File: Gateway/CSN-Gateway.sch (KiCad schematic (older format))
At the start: 42 parts, among them IC1 ATMEGA328-A, P1 CONN_DEBUG, P2 CONN_01X02, P3 CONN_ICSP, P4 CONN_OLED_SCREEN, P5 YHDC_SCT-013, P6 YHDC_SCT-013, P7 YHDC_SCT-013, P8 CONN_NRF24L01, P9 CONN_RS485, SW1 SW_PUSH, U1 MAX485CSA, U2 AMS1117-3.3, Y1 Crystal

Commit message: More work on gateway
- Add ftdi ft232rl chip for usb comms
- Remove debug connector (not used if we have usb)
- Add capa and resistors to rs485
- Draw edge cut for both bottom and top pcb at the correct size of the
case
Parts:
- removed P1: CONN_DEBUG, symbol CONN_01X06
- added C12: 0.1uF, symbol C
- added C13: 10uF, symbol C
- added IC2: FT232RL, SSOP28-LD, symbol FT232RL
- added P1: USB_MINI, symbol USB_OTG
- added R17, R18: 20K, symbol R
- added R19: 120, symbol R
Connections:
- net labels removed: DTR
- wire segments 176 -> 201
- no-connect marks 2 -> 18
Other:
- moved on the sheet: C1, C10, C11, C3, C4, C5, C6, C7, C8, C9, D1, IC1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

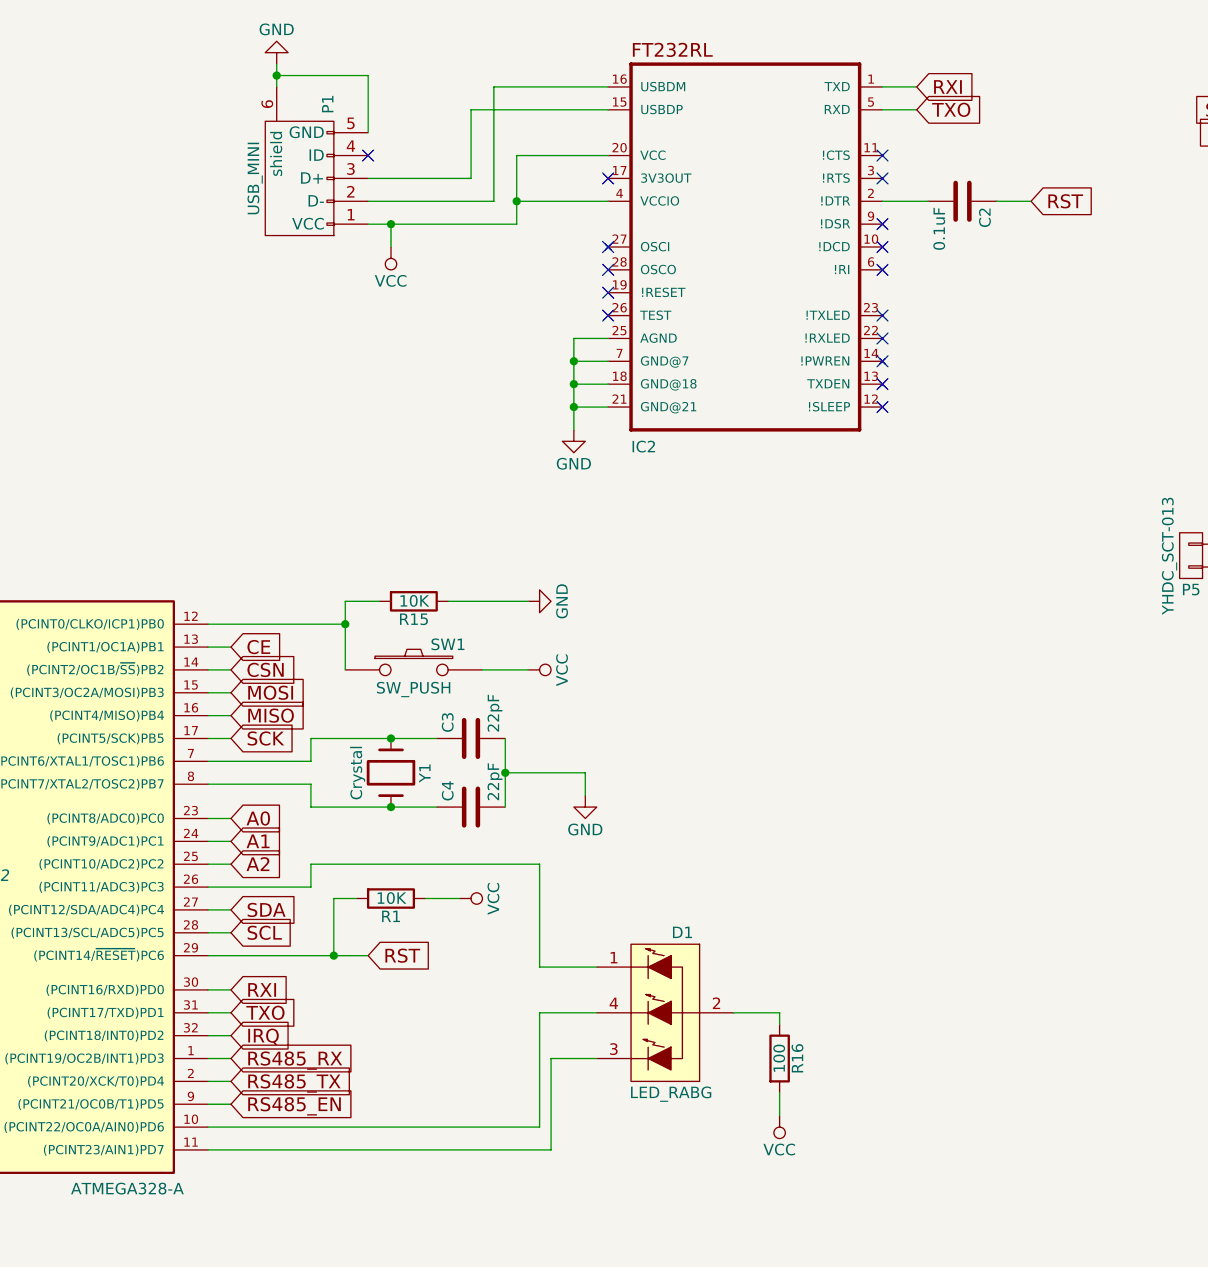
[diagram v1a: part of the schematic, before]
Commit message: FT232R in Self powered mode + switch button
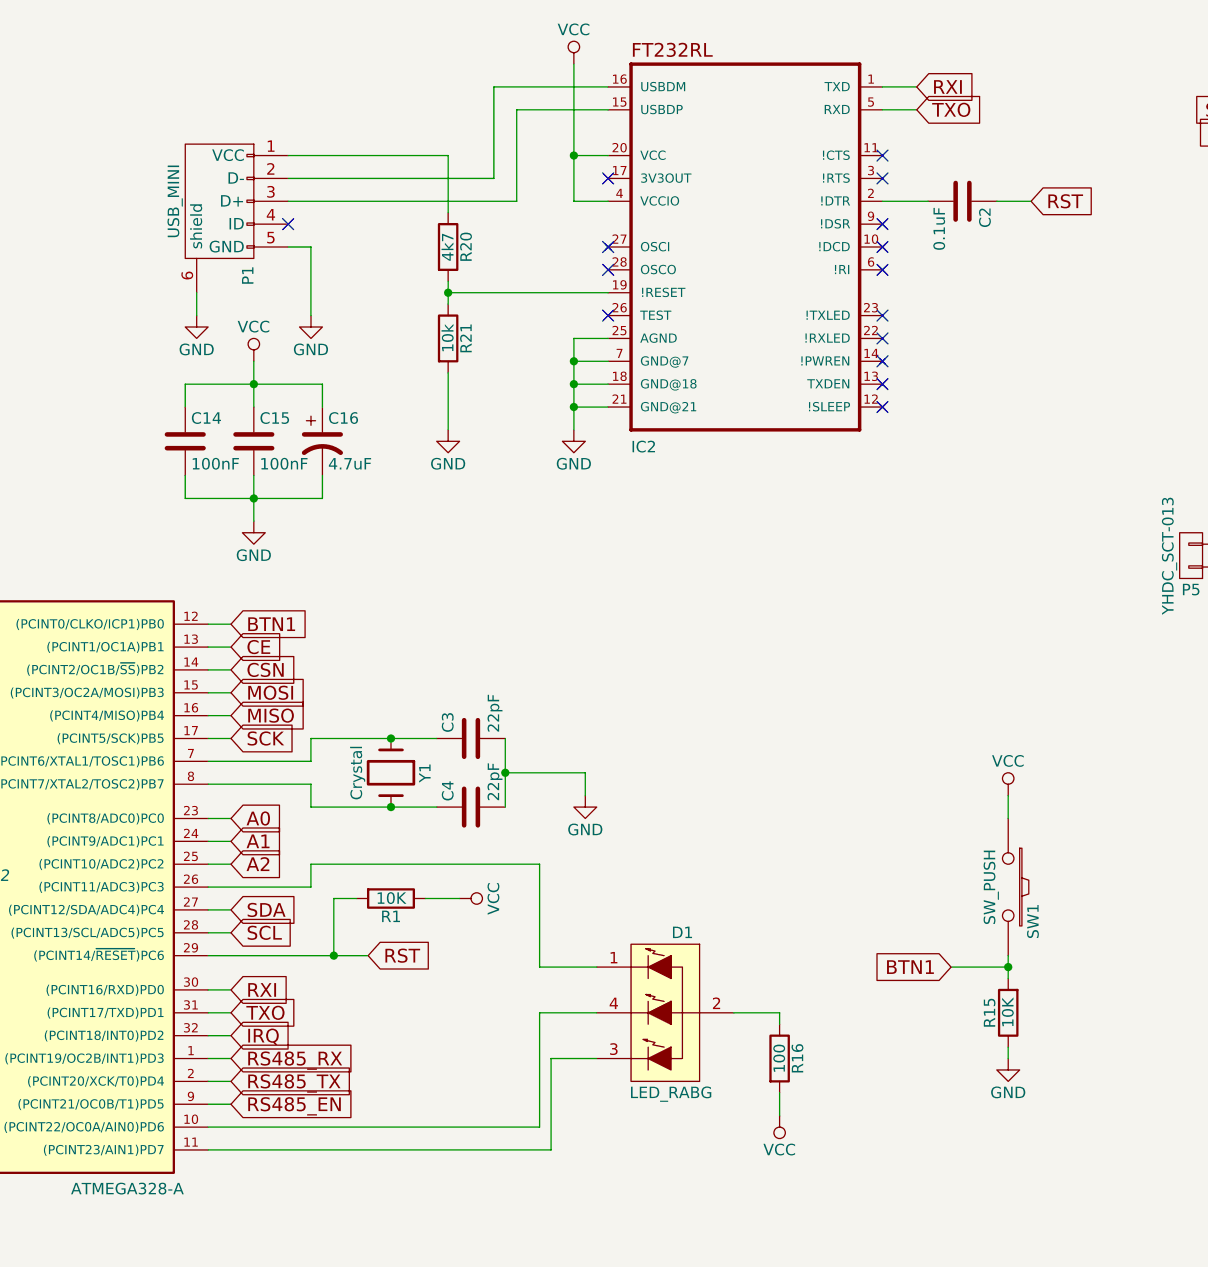
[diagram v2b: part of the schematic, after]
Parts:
- added C14, C15: 100nF, symbol C
- added C16: 4.7uF, symbol CP1
- added R20: 4k7, symbol R
- added R21: 10k, symbol R
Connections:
- net GND: now also C14.2, C15.2, C16.2, R21.2
- net VCC: now also SW1.1, C14.1, C15.1, C16.1; no longer P1.1 (VCC), SW1.2
- net BTN1: now reaches IC1.12 ((PCINT0/CLKO/ICP1)PB0), R15.2
- net BTN1: now also SW1.2; no longer SW1.1
- net at IC2.19 (!RESET): now also R20.2, R21.1
- new net: P1.1 (VCC), R20.1
- no-connect marks 18 -> 17
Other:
- moved on the sheet: P1, R15, SW1

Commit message: Change capa
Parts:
- C10, C13, C9: symbol C -> CP1
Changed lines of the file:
@@
 $EndComp
 $Comp
-L GND #PWR3
+L GND #PWR01
 U 1 1 582C3EF1
 P 1350 5550
-F 0 "#PWR3" H 1350 5300 50  0001 C CNN
+F 0 "#PWR01" H 1350 5300 50  0001 C CNN
 F 1 "GND" H 1350 5400 50  0000 C CNN
 F 2 "" H 1350 5550 50  0000 C CNN
@@
 $EndComp
 $Comp
-L GND #PWR20
+L GND #PWR02
 U 1 1 582C410C
 P 5000 3900
-F 0 "#PWR20" H 5000 3650 50  0001 C CNN
+F 0 "#PWR02" H 5000 3650 50  0001 C CNN
 F 1 "GND" H 5000 3750 50  0000 C CNN
 F 2 "" H 5000 3900 50  0000 C CNN
@@
 $EndComp
 $Comp
-L GND #PWR1
+L GND #PWR03
 U 1 1 582C5420
 P 800 4250
-F 0 "#PWR1" H 800 4000 50  0001 C CNN
+F 0 "#PWR03" H 800 4000 50  0001 C CNN
 F 1 "GND" H 800 4100 50  0000 C CNN
 F 2 "" H 800 4250 50  0000 C CNN
@@
 $EndComp
 $Comp
-L VCC #PWR2
+L VCC #PWR04
 U 1 1 582C5592
 P 1300 3050
-F 0 "#PWR2" H 1300 2900 50  0001 C CNN
+F 0 "#PWR04" H 1300 2900 50  0001 C CNN
 F 1 "VCC" H 1300 3200 50  0000 C CNN
 F 2 "" H 1300 3050 50  0000 C CNN
@@
 $EndComp
 $Comp
-L VCC #PWR15
+L VCC #PWR05
 U 1 1 582C58DF
 P 4450 4350
-F 0 "#PWR15" H 4450 4200 50  0001 C CNN
+F 0 "#PWR05" H 4450 4200 50  0001 C CNN
 F 1 "VCC" H 4450 4500 50  0000 C CNN
 F 2 "" H 4450 4350 50  0000 C CNN
@@
 TXO
 $Comp
-L PWR_FLAG #FLG1
+L PWR_FLAG #FLG06
 U 1 1 582C6C8A
 P 1350 750
-F 0 "#FLG1" H 1350 845 50  0001 C CNN
+F 0 "#FLG06" H 1350 845 50  0001 C CNN
 F 1 "PWR_FLAG" H 1350 930 50  0000 C CNN
 F 2 "" H 1350 750 50  0000 C CNN
@@
 $EndComp
 $Comp
-L VCC #PWR4
+L VCC #PWR07
 U 1 1 582C6CAE
 P 1450 800
-F 0 "#PWR4" H 1450 650 50  0001 C CNN
+F 0 "#PWR07" H 1450 650 50  0001 C CNN
 F 1 "VCC" H 1450 950 50  0000 C CNN
 F 2 "" H 1450 800 50  0000 C CNN
@@
 $EndComp
 $Comp
-L PWR_FLAG #FLG2
+L PWR_FLAG #FLG08
 U 1 1 582C6CD2
 P 1350 1150
-F 0 "#FLG2" H 1350 1245 50  0001 C CNN
+F 0 "#FLG08" H 1350 1245 50  0001 C CNN
 F 1 "PWR_FLAG" H 1350 1330 50  0000 C CNN
 F 2 "" H 1350 1150 50  0000 C CNN
@@
 $EndComp
 $Comp
-L GND #PWR5
+L GND #PWR09
 U 1 1 582C7255
 P 1450 1100
-F 0 "#PWR5" H 1450 850 50  0001 C CNN
+F 0 "#PWR09" H 1450 850 50  0001 C CNN
 F 1 "GND" H 1450 950 50  0000 C CNN
 F 2 "" H 1450 1100 50  0000 C CNN
@@
 MOSI
 $Comp
-L GND #PWR7
+L GND #PWR010
 U 1 1 582C8778
 P 1800 2250
-F 0 "#PWR7" H 1800 2000 50  0001 C CNN
+F 0 "#PWR010" H 1800 2000 50  0001 C CNN
 F 1 "GND" H 1800 2100 50  0000 C CNN
 F 2 "" H 1800 2250 50  0000 C CNN
@@
 $EndComp
 $Comp
-L VCC #PWR6
+L VCC #PWR011
 U 1 1 582C87A0
 P 1800 1950
-F 0 "#PWR6" H 1800 1800 50  0001 C CNN
+F 0 "#PWR011" H 1800 1800 50  0001 C CNN
 F 1 "VCC" H 1800 2100 50  0000 C CNN
 F 2 "" H 1800 1950 50  0000 C CNN
@@
 $EndComp
 $Comp
-L GND #PWR23
+L GND #PWR012
 U 1 1 583827DD
 P 7800 1450
-F 0 "#PWR23" H 7800 1200 50  0001 C CNN
+F 0 "#PWR012" H 7800 1200 50  0001 C CNN
 F 1 "GND" H 7800 1300 50  0000 C CNN
 F 2 "" H 7800 1450 50  0000 C CNN
@@
 $EndComp
 $Comp
-L VCC #PWR24
+L VCC #PWR013
 U 1 1 58382807
 P 8000 1450
-F 0 "#PWR24" H 8000 1300 50  0001 C CNN
+F 0 "#PWR013" H 8000 1300 50  0001 C CNN
 F 1 "VCC" H 8000 1600 50  0000 C CNN
 F 2 "" H 8000 1450 50  0000 C CNN
@@
 $EndComp
 $Comp
-L VCC #PWR25
+L VCC #PWR014
 U 1 1 58385B4B
 P 8700 2450
-F 0 "#PWR25" H 8700 2300 50  0001 C CNN
+F 0 "#PWR014" H 8700 2300 50  0001 C CNN
 F 1 "VCC" H 8700 2600 50  0000 C CNN
 F 2 "" H 8700 2450 50  0000 C CNN
@@
 $EndComp
 $Comp
-L GND #PWR26
+L GND #PWR015
 U 1 1 58385B7D
 P 8950 3600
-F 0 "#PWR26" H 8950 3350 50  0001 C CNN
+F 0 "#PWR015" H 8950 3350 50  0001 C CNN
 F 1 "GND" H 8950 3450 50  0000 C CNN
 F 2 "" H 8950 3600 50  0000 C CNN
@@
 $EndComp
 $Comp
-L VCC #PWR31
+L VCC #PWR016
 U 1 1 58387833
 P 10650 2450
-F 0 "#PWR31" H 10650 2300 50  0001 C CNN
+F 0 "#PWR016" H 10650 2300 50  0001 C CNN
 F 1 "VCC" H 10650 2600 50  0000 C CNN
 F 2 "" H 10650 2450 50  0000 C CNN
@@
 $EndComp
 $Comp
-L GND #PWR33
+L GND #PWR017
 U 1 1 58387839
 P 10900 3600
-F 0 "#PWR33" H 10900 3350 50  0001 C CNN
+F 0 "#PWR017" H 10900 3350 50  0001 C CNN
 F 1 "GND" H 10900 3450 50  0000 C CNN
 F 2 "" H 10900 3600 50  0000 C CNN
@@
 $EndComp
 $Comp
-L VCC #PWR30
+L VCC #PWR018
 U 1 1 58387BF8
 P 10650 850
-F 0 "#PWR30" H 10650 700 50  0001 C CNN
+F 0 "#PWR018" H 10650 700 50  0001 C CNN
 F 1 "VCC" H 10650 1000 50  0000 C CNN
 F 2 "" H 10650 850 50  0000 C CNN
@@
 $EndComp
 $Comp
-L GND #PWR32
+L GND #PWR019
 U 1 1 58387BFE
 P 10900 2000
-F 0 "#PWR32" H 10900 1750 50  0001 C CNN
+F 0 "#PWR019" H 10900 1750 50  0001 C CNN
 F 1 "GND" H 10900 1850 50  0000 C CNN
 F 2 "" H 10900 2000 50  0000 C CNN
@@
 $EndComp
 $Comp
-L GND #PWR28
+L GND #PWR020
 U 1 1 5838AB1A
 P 9450 6200
-F 0 "#PWR28" H 9450 5950 50  0001 C CNN
+F 0 "#PWR020" H 9450 5950 50  0001 C CNN
 F 1 "GND" H 9450 6050 50  0000 C CNN
 F 2 "" H 9450 6200 50  0000 C CNN
@@
 $EndComp
 $Comp
-L VCC #PWR27
+L VCC #PWR021
 U 1 1 5838AD80
 P 9450 4400
-F 0 "#PWR27" H 9450 4250 50  0001 C CNN
+F 0 "#PWR021" H 9450 4250 50  0001 C CNN
 F 1 "VCC" H 9450 4550 50  0000 C CNN
 F 2 "" H 9450 4400 50  0000 C CNN
@@
 $EndComp
 $Comp
-L VCC #PWR8
+L VCC #PWR022
 U 1 1 58394BCB
 P 1850 6300
-F 0 "#PWR8" H 1850 6150 50  0001 C CNN
+F 0 "#PWR022" H 1850 6150 50  0001 C CNN
 F 1 "VCC" H 1850 6450 50  0000 C CNN
 F 2 "" H 1850 6300 50  0000 C CNN
@@
 $EndComp
 $Comp
-L GND #PWR21
+L GND #PWR023
 U 1 1 58394C21
 P 5650 7300
-F 0 "#PWR21" H 5650 7050 50  0001 C CNN
+F 0 "#PWR023" H 5650 7050 50  0001 C CNN
 F 1 "GND" H 5650 7150 50  0000 C CNN
 F 2 "" H 5650 7300 50  0000 C CNN
@@
 $EndComp
 $Comp
-L GND #PWR16
+L GND #PWR024
 U 1 1 5839D6E3
 P 6850 5050
-F 0 "#PWR16" H 6850 4800 50  0001 C CNN
+F 0 "#PWR024" H 6850 4800 50  0001 C CNN
 F 1 "GND" H 6850 4900 50  0000 C CNN
 F 2 "" H 6850 5050 50  0000 C CNN
@@
 $EndComp
 $Comp
-L VCC #PWR17
+L VCC #PWR025
 U 1 1 5839D82D
 P 6850 3900
-F 0 "#PWR17" H 6850 3750 50  0001 C CNN
+F 0 "#PWR025" H 6850 3750 50  0001 C CNN
 F 1 "VCC" H 6850 4050 50  0000 C CNN
 F 2 "" H 6850 3900 50  0000 C CNN
@@
 $EndComp
 $Comp
-L VCC #PWR22
+L VCC #PWR026
 U 1 1 5839F258
 P 5850 5300
-F 0 "#PWR22" H 5850 5150 50  0001 C CNN
+F 0 "#PWR026" H 5850 5150 50  0001 C CNN
 F 1 "VCC" H 5850 5450 50  0000 C CNN
 F 2 "" H 5850 5300 50  0000 C CNN
@@
 $EndComp
 $Comp
-L GND #PWR9
+L GND #PWR027
 U 1 1 583A146D
 P 2900 7400
-F 0 "#PWR9" H 2900 7150 50  0001 C CNN
+F 0 "#PWR027" H 2900 7150 50  0001 C CNN
 F 1 "GND" H 2900 7250 50  0000 C CNN
 F 2 "" H 2900 7400 50  0000 C CNN
@@
 $EndComp
 $Comp
-L C C9
+L CP1 C9
 U 1 1 583A24B0
 P 3450 6900
@@
 $EndComp
 $Comp
-L C C10
+L CP1 C10
 U 1 1 583A3B3C
 P 1900 6900
@@
 $EndComp
 $Comp
-L C C13
+L CP1 C13
 U 1 1 583B1742
 P 9650 5050
@@
 $EndComp
 $Comp
-L GND #PWR29
+L GND #PWR028
 U 1 1 583B1A4D
 P 9900 4900
-F 0 "#PWR29" H 9900 4650 50  0001 C CNN
+F 0 "#PWR028" H 9900 4650 50  0001 C CNN
 F 1 "GND" H 9900 4750 50  0000 C CNN
 F 2 "" H 9900 4900 50  0000 C CNN
@@
 $EndComp
 $Comp
-L GND #PWR13
+L GND #PWR029
 U 1 1 583B4E1D
 P 3800 1800
-F 0 "#PWR13" H 3800 1550 50  0001 C CNN
+F 0 "#PWR029" H 3800 1550 50  0001 C CNN
 F 1 "GND" H 3800 1650 50  0000 C CNN
 F 2 "" H 3800 1800 50  0000 C CNN
@@
 NoConn ~ 5100 1800
 $Comp
-L GND #PWR19
+L GND #PWR030
 U 1 1 583B84FE
 P 4950 2300
-F 0 "#PWR19" H 4950 2050 50  0001 C CNN
+F 0 "#PWR030" H 4950 2050 50  0001 C CNN
 F 1 "GND" H 4950 2150 50  0000 C CNN
 F 2 "" H 4950 2300 50  0000 C CNN
@@
 	4400 1100 4400 1350
 $Comp
-L GND #PWR14
+L GND #PWR031
 U 1 1 583B546D
 P 4400 2300
-F 0 "#PWR14" H 4400 2050 50  0001 C CNN
+F 0 "#PWR031" H 4400 2050 50  0001 C CNN
 F 1 "GND" H 4400 2150 50  0000 C CNN
 F 2 "" H 4400 2300 50  0000 C CNN
@@
 	4700 900  5100 900
 $Comp
-L VCC #PWR18
+L VCC #PWR032
 U 1 1 583B5BC5
 P 4950 700
-F 0 "#PWR18" H 4950 550 50  0001 C CNN
+F 0 "#PWR032" H 4950 550 50  0001 C CNN
 F 1 "VCC" H 4950 850 50  0000 C CNN
 F 2 "" H 4950 700 50  0000 C CNN
@@
 NoConn ~ 3700 1400
 $Comp
-L GND #PWR10
+L GND #PWR033
 U 1 1 583B65C5
 P 3300 1800
-F 0 "#PWR10" H 3300 1550 50  0001 C CNN
+F 0 "#PWR033" H 3300 1550 50  0001 C CNN
 F 1 "GND" H 3300 1650 50  0000 C CNN
 F 2 "" H 3300 1800 50  0000 C CNN
@@
 Connection ~ 3550 2100
 $Comp
-L GND #PWR12
+L GND #PWR034
 U 1 1 583B7215
 P 3550 2700
-F 0 "#PWR12" H 3550 2450 50  0001 C CNN
+F 0 "#PWR034" H 3550 2450 50  0001 C CNN
 F 1 "GND" H 3550 2550 50  0000 C CNN
 F 2 "" H 3550 2700 50  0000 C CNN
@@
 $EndComp
 $Comp
-L VCC #PWR11
+L VCC #PWR035
 U 1 1 583B7400
 P 3550 2000
-F 0 "#PWR11" H 3550 1850 50  0001 C CNN
+F 0 "#PWR035" H 3550 1850 50  0001 C CNN
 F 1 "VCC" H 3550 2150 50  0000 C CNN
 F 2 "" H 3550 2000 50  0000 C CNN

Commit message: Finish gateway power supply
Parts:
- removed C16: 4.7uF, symbol CP1
- removed U2: AMS1117-3.3, SOT-223, symbol AMS1117-3.3
- added C16, C18: 100nF, symbol C
- added C17: 10uF, symbol CP1
- added D2: TL431, symbol TL431
- added Q1: 2N2222, symbol Q_NPN_BCE
- added R22, R23: 100, symbol R
- added R24: 1.5K, symbol R
- added R25, R26: 27.4K, symbol R
- added R27: 10K, symbol R
- added SW2: SW_PUSH, symbol SW_PUSH
- added U2: AMS1117-3.3V, symbol AMS1117
- added U3: ATSHA204A, SOT-23_Handsoldering, symbol ATSHA204A
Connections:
- net A2: now also IC1.19 (ADC6); no longer IC1.25 ((PCINT10/ADC2)PC2)
- net GND: now also C16.2, C17.2, C18.2, D2.2 (A), R26.2, R27.1, U2.1 (GND), U3.3 (GND)
- net SDA: now also U3.1 (SDA)
- net VCC: now also D1.2 (COMMON_ANODE), R20.1, C17.1, C18.1, Q1.3 (E), R25.1, SW2.1, U2.3 (VI), U3.2 (VCC); no longer P2.2 (P2), R16.2
- net at IC1.10 ((PCINT22/OC0A/AIN0)PD6): now also R22.1; no longer D1.4 (GREEN_CATHODE)
- net at IC1.11 ((PCINT23/AIN1)PD7): now also R23.1; no longer D1.3 (BLUE_CATHODE)
- net at IC1.26 ((PCINT11/ADC3)PC3): now also R16.1; no longer D1.1 (RED_CATHODE)
- net at C11.1, C9.1, P8.7 (P7): now also U2.2 (VO)
- net at P1.1 (VCC): no longer R20.1
- new net: P2.2 (P2), Q1.2 (C), R24.1
- new net: D1.1 (RED_CATHODE), R16.2
- new net: D1.3 (BLUE_CATHODE), R23.2
- new net: D1.4 (GREEN_CATHODE), R22.2
- new net: D2.1 (K), Q1.1 (B), R24.2
- new net: C16.1, D2.3 (Ref), R25.2, R26.1
- new net BTN2: IC1.25 ((PCINT10/ADC2)PC2), R27.2, SW2.2
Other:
- note added: "R24 = (Vin - 5.6V) / I\nI = 10mA for 24V\nImin for 5V = 5mA"
- moved on the sheet: C10, C11, C14, C15, C5, C6, C7, C8, C9, D1, P1, P2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
